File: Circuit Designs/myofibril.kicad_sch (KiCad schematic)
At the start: 66 parts, among them Q3 CSD87384M, Q4 CSD87384M, Q5 CSD87384M, T2 B3380, U10 INA199A1, U8 INA199A1, U9 INA199A1

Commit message: done all the packages and migrations. Now, time to start to route the module
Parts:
- Q3, Q4, Q5: value CSD87384M -> BUK7V4R2; footprint (none) -> CoF_SmallOutline:SOT-1205; symbol CoE-Transistor:CSD87384M -> CoE-Transistor:BUK7V4R2; Digikey Part # 296-CSD87384MCT-ND -> 1727-BUK7V4R2-40HXCT-ND; Farnell Part # (none) -> 3677633; MFR. Part # CSD87384M -> BUK7V4R2; Mouser Part # 595-CSD87384M -> (none); VDS 24V -> 40V
- U10, U8, U9: footprint Package_TO_SOT_SMD:Texas_R-PDSO-G6 -> CoF_SmallOutline:SOT-363
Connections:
- net at R71.1: now also Q3.6 (S1/D2); no longer Q3.3 (S1/D2)
- net at R72.1: now also Q4.6 (S1/D2); no longer Q4.3 (S1/D2)
- net at R73.1: now also Q5.6 (S1/D2); no longer Q5.3 (S1/D2)

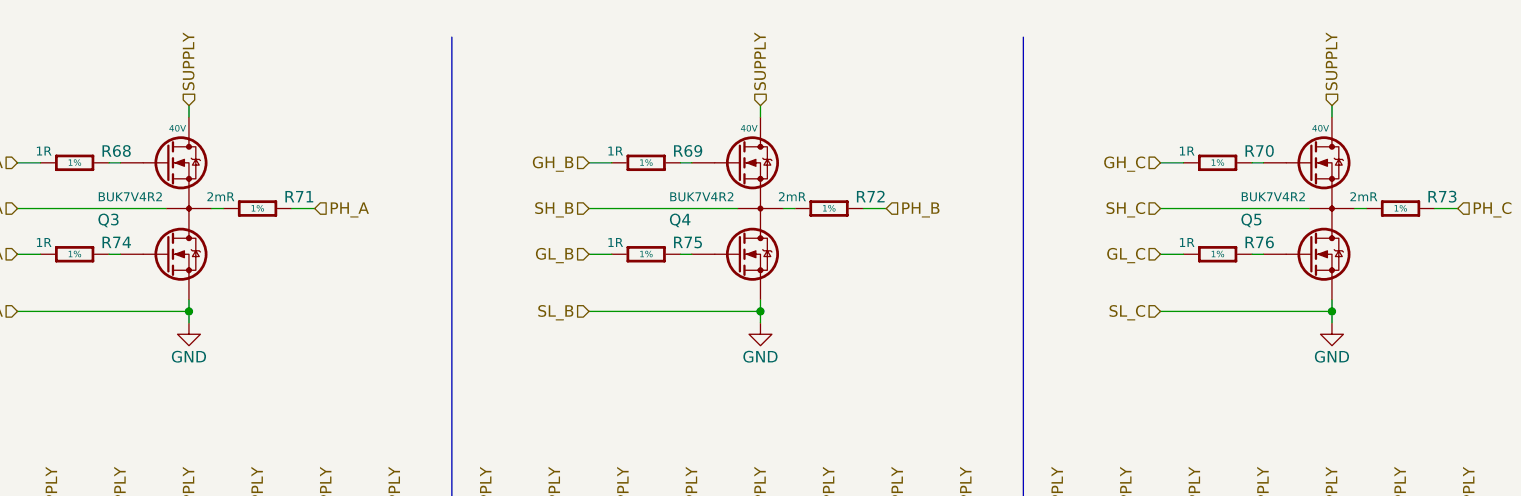
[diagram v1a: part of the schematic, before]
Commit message: placed LEDs, mosfets, bulk capacitors
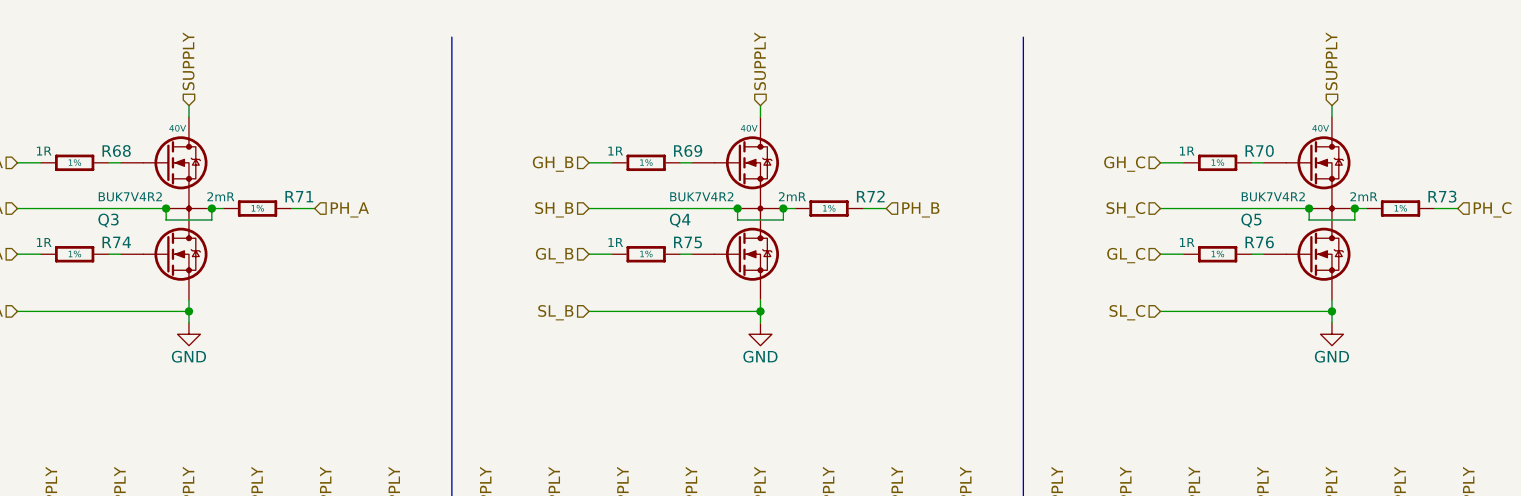
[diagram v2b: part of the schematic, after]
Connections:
- net SH_A: now also Q3.6 (S1/D2), R71.1
- net SH_B: now also Q4.6 (S1/D2), R72.1
- net SH_C: now also Q5.6 (S1/D2), R73.1
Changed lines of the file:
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@@
     (comment 4 "The pectoralis is a large muscle that attaches to the humerus of the wing ")
   )
+  (junction (at 209.55 38.1) (diameter 0) (color 0 0 0 0)
+  )
   (junction (at 205.74 149.86) (diameter 0) (color 0 0 0 0)
   )
@@
   (junction (at 31.75 179.07) (diameter 0) (color 0 0 0 0)
   )
+  (junction (at 214.63 38.1) (diameter 0) (color 0 0 0 0)
+  )
   (junction (at 218.44 115.57) (diameter 0) (color 0 0 0 0)
   )
   (junction (at 212.09 49.53) (diameter 0) (color 0 0 0 0)
   )
+  (junction (at 146.05 38.1) (diameter 0) (color 0 0 0 0)
+  )
   (junction (at 91.44 115.57) (diameter 0) (color 0 0 0 0)
   )
+  (junction (at 87.63 38.1) (diameter 0) (color 0 0 0 0)
+  )
   (junction (at 148.59 49.53) (diameter 0) (color 0 0 0 0)
   )
+  (junction (at 151.13 38.1) (diameter 0) (color 0 0 0 0)
+  )
   (junction (at 85.09 49.53) (diameter 0) (color 0 0 0 0)
   )
@@
   )
   (junction (at 59.69 115.57) (diameter 0) (color 0 0 0 0)
+  )
+  (junction (at 82.55 38.1) (diameter 0) (color 0 0 0 0)
   )
   (junction (at 218.44 125.73) (diameter 0) (color 0 0 0 0)
@@
     (stroke (width 0) (type default) (color 0 0 0 0))
   )
+  (wire (pts (xy 214.63 39.37) (xy 214.63 38.1))
+    (stroke (width 0) (type default) (color 0 0 0 0))
+  )
   (wire (pts (xy 212.09 26.67) (xy 212.09 27.94))
     (stroke (width 0) (type default) (color 0 0 0 0))
@@
     (stroke (width 0) (type default) (color 0 0 0 0))
   )
+  (wire (pts (xy 87.63 39.37) (xy 87.63 38.1))
+    (stroke (width 0) (type default) (color 0 0 0 0))
+  )
   (wire (pts (xy 194.31 149.86) (xy 193.04 149.86))
     (stroke (width 0) (type default) (color 0 0 0 0))
@@
     (stroke (width 0) (type default) (color 0 0 0 0))
   )
+  (wire (pts (xy 209.55 38.1) (xy 209.55 39.37))
+    (stroke (width 0) (type default) (color 0 0 0 0))
+  )
   (wire (pts (xy 201.93 144.78) (xy 205.74 144.78))
     (stroke (width 0) (type default) (color 0 0 0 0))
@@
     (stroke (width 0) (type default) (color 0 0 0 0))
   )
+  (wire (pts (xy 151.13 39.37) (xy 151.13 38.1))
+    (stroke (width 0) (type default) (color 0 0 0 0))
+  )
   (wire (pts (xy 160.02 38.1) (xy 162.56 38.1))
     (stroke (width 0) (type default) (color 0 0 0 0))
@@
     (stroke (width 0) (type default) (color 0 0 0 0))
   )
+  (wire (pts (xy 82.55 39.37) (xy 87.63 39.37))
+    (stroke (width 0) (type default) (color 0 0 0 0))
+  )
   (wire (pts (xy 118.11 74.93) (xy 118.11 76.2))
     (stroke (width 0) (type default) (color 0 0 0 0))
@@
     (stroke (width 0) (type default) (color 0 0 0 0))
   )
+  (wire (pts (xy 209.55 39.37) (xy 214.63 39.37))
+    (stroke (width 0) (type default) (color 0 0 0 0))
+  )
   (wire (pts (xy 234.95 74.93) (xy 234.95 76.2))
     (stroke (width 0) (type default) (color 0 0 0 0))
@@
     (stroke (width 0) (type default) (color 0 0 0 0))
   )
+  (wire (pts (xy 82.55 38.1) (xy 82.55 39.37))
+    (stroke (width 0) (type default) (color 0 0 0 0))
+  )
   (wire (pts (xy 91.44 114.3) (xy 91.44 115.57))
     (stroke (width 0) (type default) (color 0 0 0 0))
@@
     (stroke (width 0) (type default) (color 0 0 0 0))
   )
+  (wire (pts (xy 146.05 38.1) (xy 146.05 39.37))
+    (stroke (width 0) (type default) (color 0 0 0 0))
+  )
   (wire (pts (xy 100.33 85.09) (xy 100.33 83.82))
     (stroke (width 0) (type default) (color 0 0 0 0))
@@
     (stroke (width 0) (type default) (color 0 0 0 0))
   )
+  (wire (pts (xy 146.05 39.37) (xy 151.13 39.37))
+    (stroke (width 0) (type default) (color 0 0 0 0))
+  )

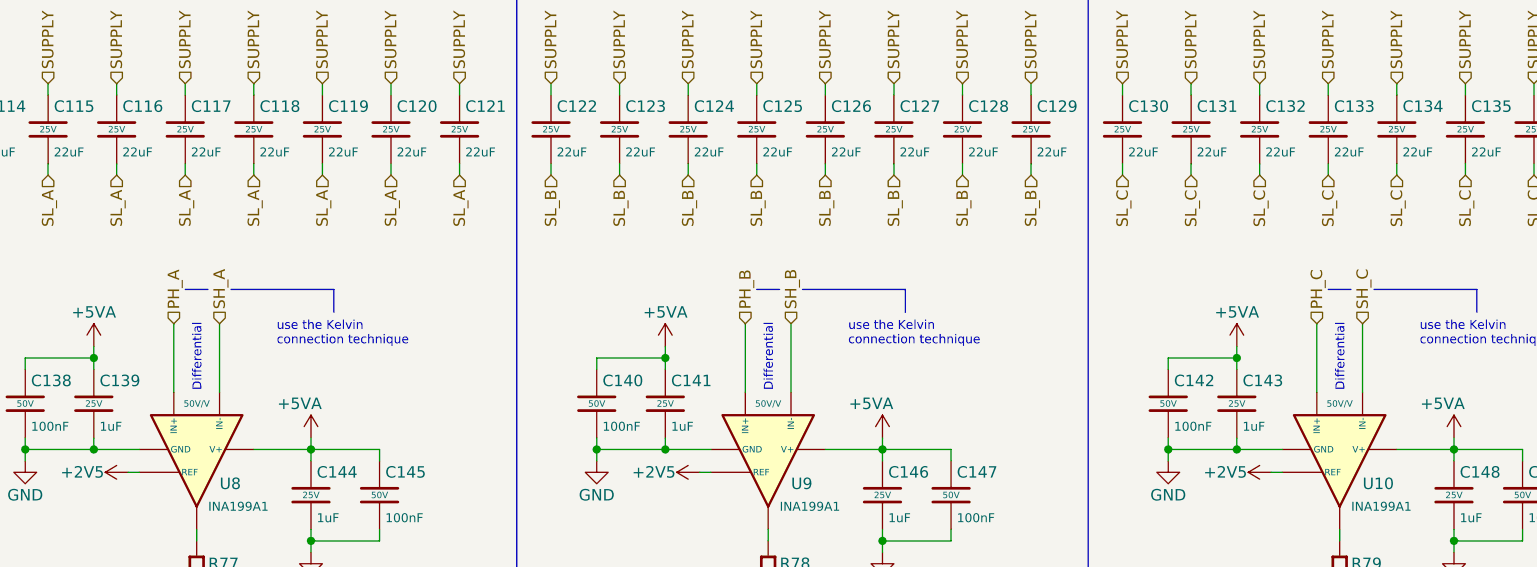
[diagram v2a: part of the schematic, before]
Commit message: placed current shunt circuits and mosfets
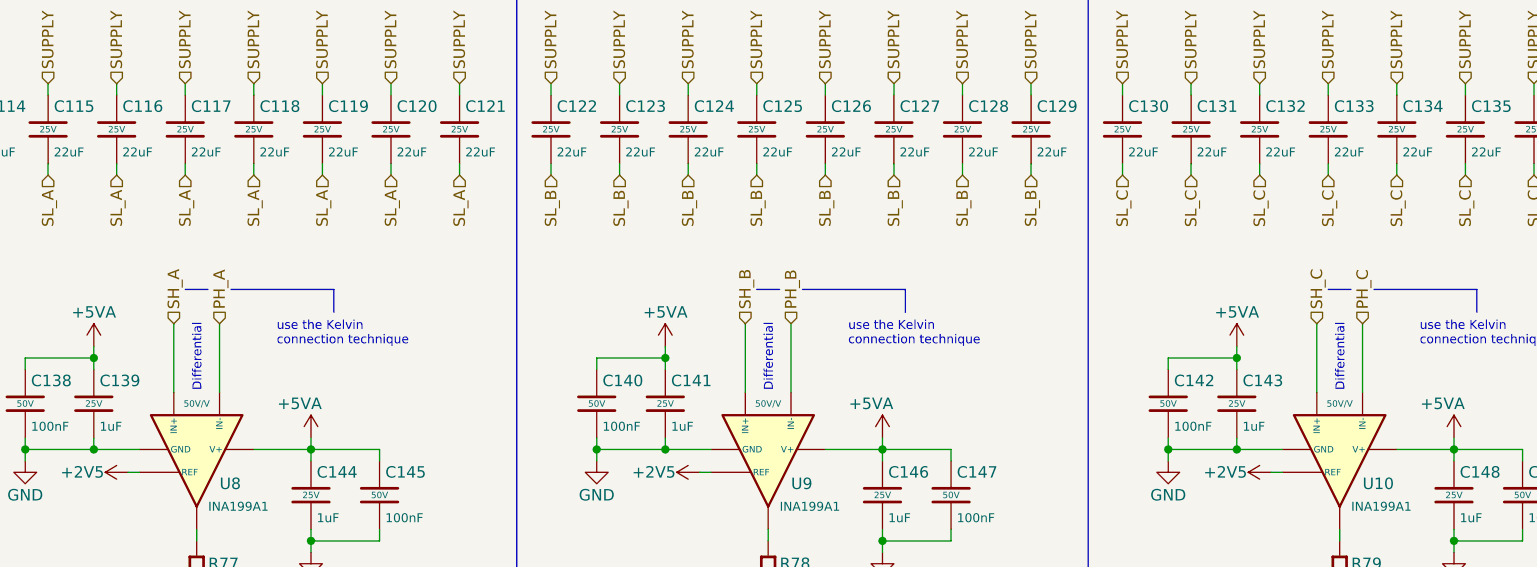
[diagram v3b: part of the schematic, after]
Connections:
- net PH_A: now also U8.5 (IN-); no longer U8.4 (IN+)
- net PH_B: now also U9.5 (IN-); no longer U9.4 (IN+)
- net PH_C: now also U10.5 (IN-); no longer U10.4 (IN+)
- net SH_A: now also U8.4 (IN+); no longer U8.5 (IN-)
- net SH_B: now also U9.4 (IN+); no longer U9.5 (IN-)
- net SH_C: now also U10.4 (IN+); no longer U10.5 (IN-)
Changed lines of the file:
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@@
     (effects (font (size 1.27 1.27)) (justify right))
   )
-  (hierarchical_label "PH_C" (shape input) (at 203.2 101.6 90)
+  (hierarchical_label "PH_C" (shape input) (at 208.28 101.6 90)
     (effects (font (size 1.27 1.27)) (justify left))
   )
@@
     (effects (font (size 1.27 1.27)) (justify left))
   )
-  (hierarchical_label "SH_C" (shape input) (at 208.28 101.6 90)
+  (hierarchical_label "SH_C" (shape input) (at 203.2 101.6 90)
     (effects (font (size 1.27 1.27)) (justify left))
   )
@@
     (effects (font (size 1.27 1.27)) (justify left))
   )
-  (hierarchical_label "PH_A" (shape input) (at 76.2 101.6 90)
+  (hierarchical_label "PH_A" (shape input) (at 81.28 101.6 90)
     (effects (font (size 1.27 1.27)) (justify left))
   )
@@
     (effects (font (size 1.27 1.27)) (justify right))
   )
-  (hierarchical_label "SH_A" (shape input) (at 81.28 101.6 90)
+  (hierarchical_label "SH_A" (shape input) (at 76.2 101.6 90)
     (effects (font (size 1.27 1.27)) (justify left))
   )
@@
     (effects (font (size 1.27 1.27)) (justify right))
   )
-  (hierarchical_label "SH_B" (shape input) (at 144.78 101.6 90)
+  (hierarchical_label "SH_B" (shape input) (at 139.7 101.6 90)
     (effects (font (size 1.27 1.27)) (justify left))
   )
@@
     (effects (font (size 1.27 1.27)) (justify right))
   )
-  (hierarchical_label "PH_B" (shape input) (at 139.7 101.6 90)
+  (hierarchical_label "PH_B" (shape input) (at 144.78 101.6 90)
     (effects (font (size 1.27 1.27)) (justify left))
   )
